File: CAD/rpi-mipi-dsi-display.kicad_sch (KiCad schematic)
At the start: 25 parts, among them J1 Conn_02x20_Odd_Even, J2 Conn_01x40, J3 Conn_01x22, U1 AMS1117-1.8, U2 TPS61165DBV

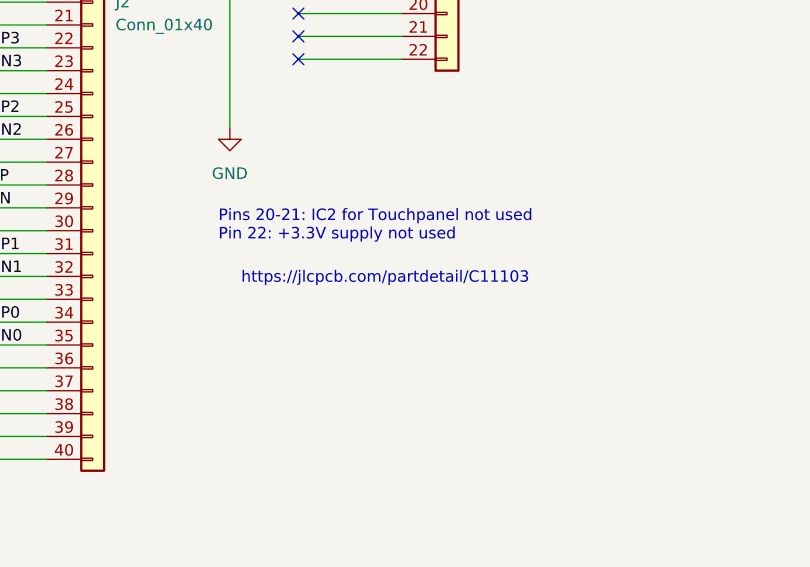
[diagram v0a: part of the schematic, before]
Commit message: Updated CAD file names
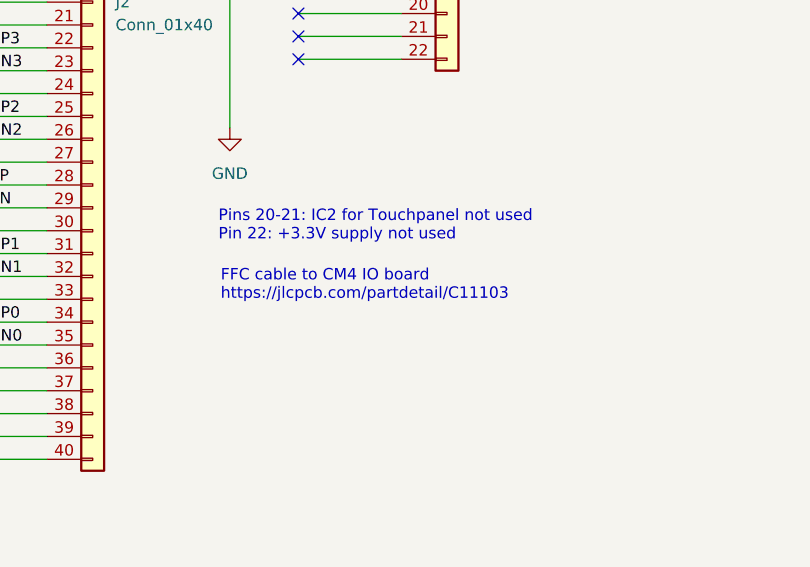
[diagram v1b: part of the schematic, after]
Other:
- note added: "FFC cable to CM4 IO board https://jlcpcb.com/partdetail/C11103"
- note removed: "https://jlcpcb.com/partdetail/C11103"
- title: (none) -> rpi-mipi-dsi-display
